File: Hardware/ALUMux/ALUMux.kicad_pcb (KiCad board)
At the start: 4 copper layers, 71.1 x 43.2 mm, 35 parts, among them J1 connector_2x8, J2 connector_2x8, J3 connector_2x8, U2MUX1 74x157, U2MUX2 74x157, U2MUX3 74x157, U2MUX4 74x157, U4MUX1 74x153, U4MUX2 74x153, U4MUX3 74x153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

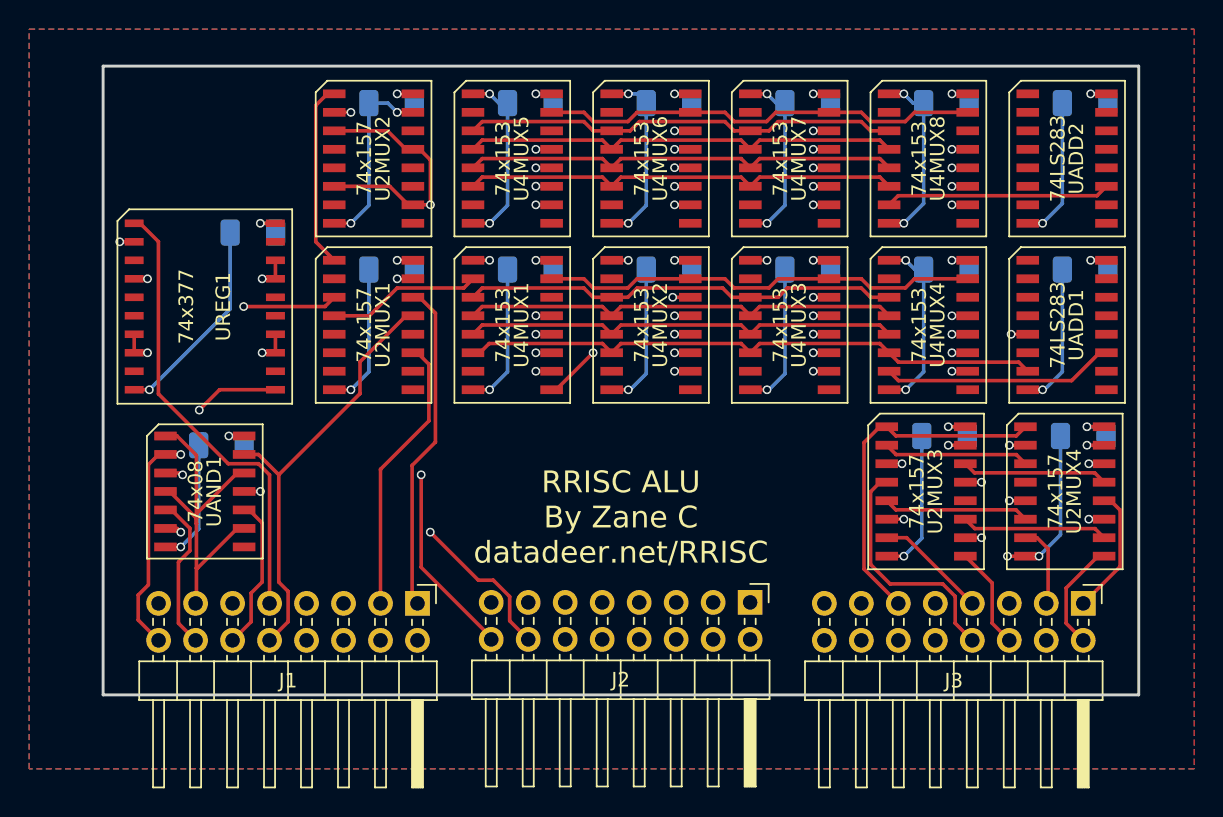
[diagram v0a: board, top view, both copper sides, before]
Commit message: ALUMux: PCB done.
Going to start ProgramCounter2
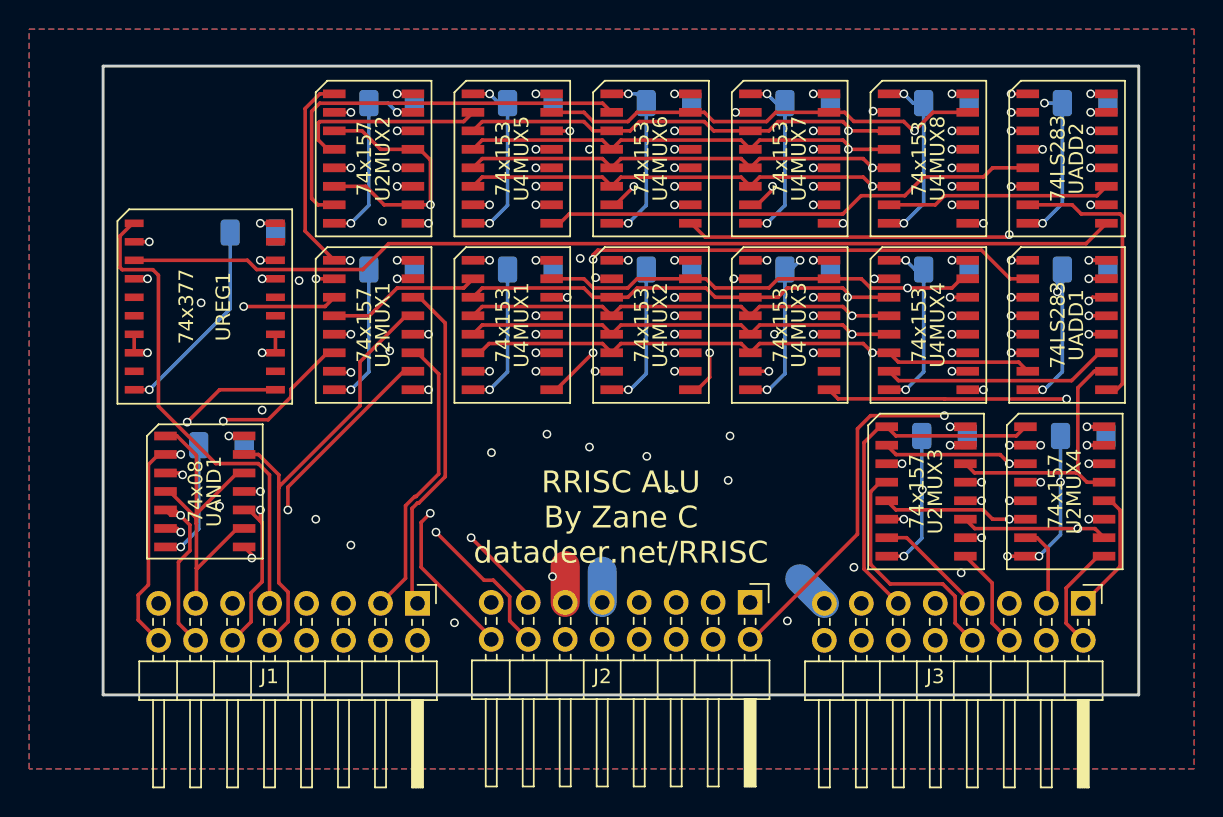
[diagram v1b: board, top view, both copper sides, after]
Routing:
- net Net-(UADD2-Pad9): track 0.00 -> 68.3 mm
- net /IN_ACC7: track 0.00 -> 44.4 mm, vias 0 -> 1
- net /ADD_RIGHT1: track 0.00 -> 40.5 mm, vias 0 -> 2
- net /IN_R3: track 60.3 -> 99.0 mm, vias 0 -> 2
- net /ADD_RIGHT4: track 0.00 -> 38.6 mm, vias 0 -> 2
- net /ADD_RIGHT0: track 0.00 -> 38.6 mm, vias 0 -> 2
- net /IN_REGDATA7: track 0.00 -> 37.8 mm, vias 0 -> 1
- net /OPB7: track 0.00 -> 36.9 mm, vias 0 -> 2
- net /IN_ACC4: track 0.00 -> 35.6 mm, vias 0 -> 1
- net /IN_R2: track 60.3 -> 95.4 mm, vias 0 -> 2
- net /OPB3: track 0.00 -> 34.9 mm, vias 0 -> 2
- net /IN_R1: track 60.3 -> 95.0 mm, vias 0 -> 2
- net /IN_REGDATA5: track 0.00 -> 34.4 mm, vias 0 -> 1
- net /ADD_LEFT4: track 0.00 -> 33.7 mm
- net /IN_R0: track 70.3 -> 104.0 mm, vias 0 -> 2
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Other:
- board text added: "Immediate"
- board text added: "In Acc"
- board text added: "Op"
- board text added: "OutRX"
- board text added: "Regdata"
- board text added: "Result"
